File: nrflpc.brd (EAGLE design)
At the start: 67.9 x 42 mm, 74 parts, among them IC1 LPC1111/12/13/14-HVQFN33, IC2 LT1763CS8-3.3, IC3 LM3401, IC5 LM3401, IC6 LM3401, IC7 LM3401, Q1 20MHz, Q2 MOSFET-PCHANNEL, Q3 MOSFET-PCHANNEL, Q4 MOSFET-PCHANNEL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

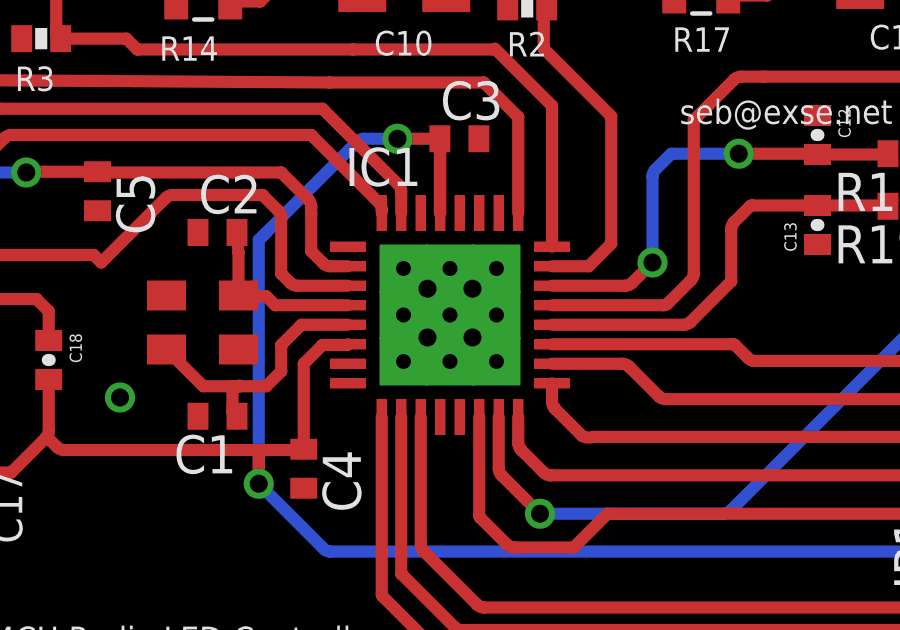
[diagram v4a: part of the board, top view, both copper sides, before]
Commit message: updated HVQFN33 package
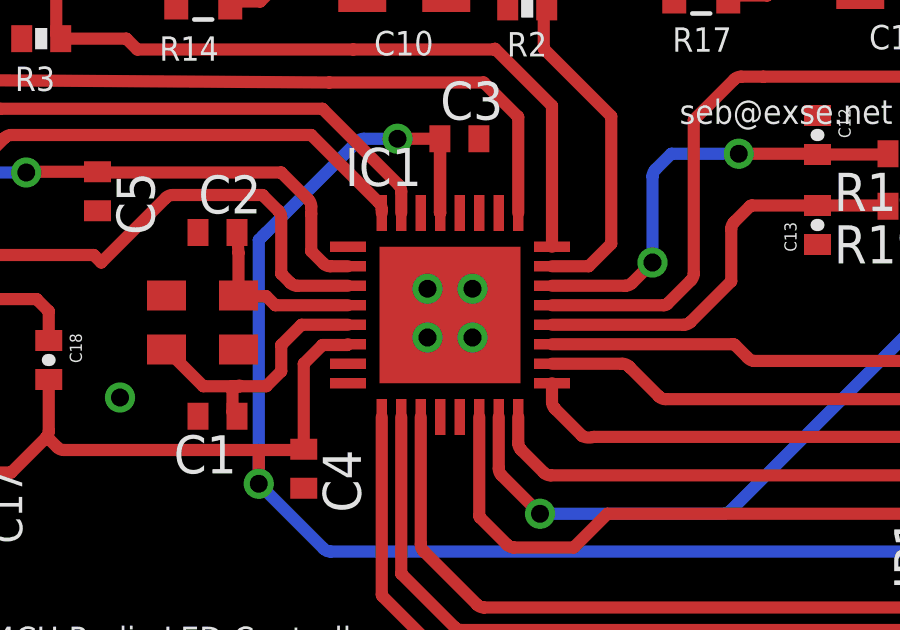
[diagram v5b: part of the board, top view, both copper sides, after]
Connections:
- net GND: now also IC1.GND; no longer IC1.33
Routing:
- net GND: track 17.8 -> 19.3 mm
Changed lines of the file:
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@@
 <contactref element="C2" pad="1"/>
 <contactref element="C1" pad="2"/>
-<contactref element="IC1" pad="33"/>
+<contactref element="IC1" pad="GND"/>
 <contactref element="C4" pad="2"/>
 <contactref element="C3" pad="2"/>
@@
 <contactref element="EXT" pad="7"/>
 <via x="21.625" y="6" extent="1-16" drill="0.6"/>
-<wire x1="32.625" y1="8.75" x2="33.375" y2="9.625" width="0" layer="19" extent="1-1"/>
-<wire x1="33.375" y1="8" x2="32.625" y2="8.75" width="0" layer="19" extent="1-1"/>
-<wire x1="31.875" y1="8" x2="32.625" y2="8.75" width="0" layer="19" extent="1-1"/>
-<wire x1="31.875" y1="9.625" x2="32.625" y2="8.75" width="0" layer="19" extent="1-1"/>
-<wire x1="33.5875" y1="14.625" x2="33.375" y2="9.625" width="0" layer="19" extent="1-1"/>
-<wire x1="34.549" y1="19.0205" x2="33.5875" y2="14.625" width="0" layer="19" extent="1-1"/>
 <wire x1="44.875" y1="11.1" x2="44.875" y2="15.4" width="0" layer="19" extent="1-1"/>
+<wire x1="33.5875" y1="14.625" x2="34.549" y2="19.0205" width="0" layer="19" extent="1-1"/>
+<wire x1="32.625" y1="8.75" x2="31.875" y2="8.75" width="0.4064" layer="1"/>
+<wire x1="31.875" y1="8.75" x2="31.875" y2="8" width="0.4064" layer="1"/>
 </signal>
 <signal name="N$1">

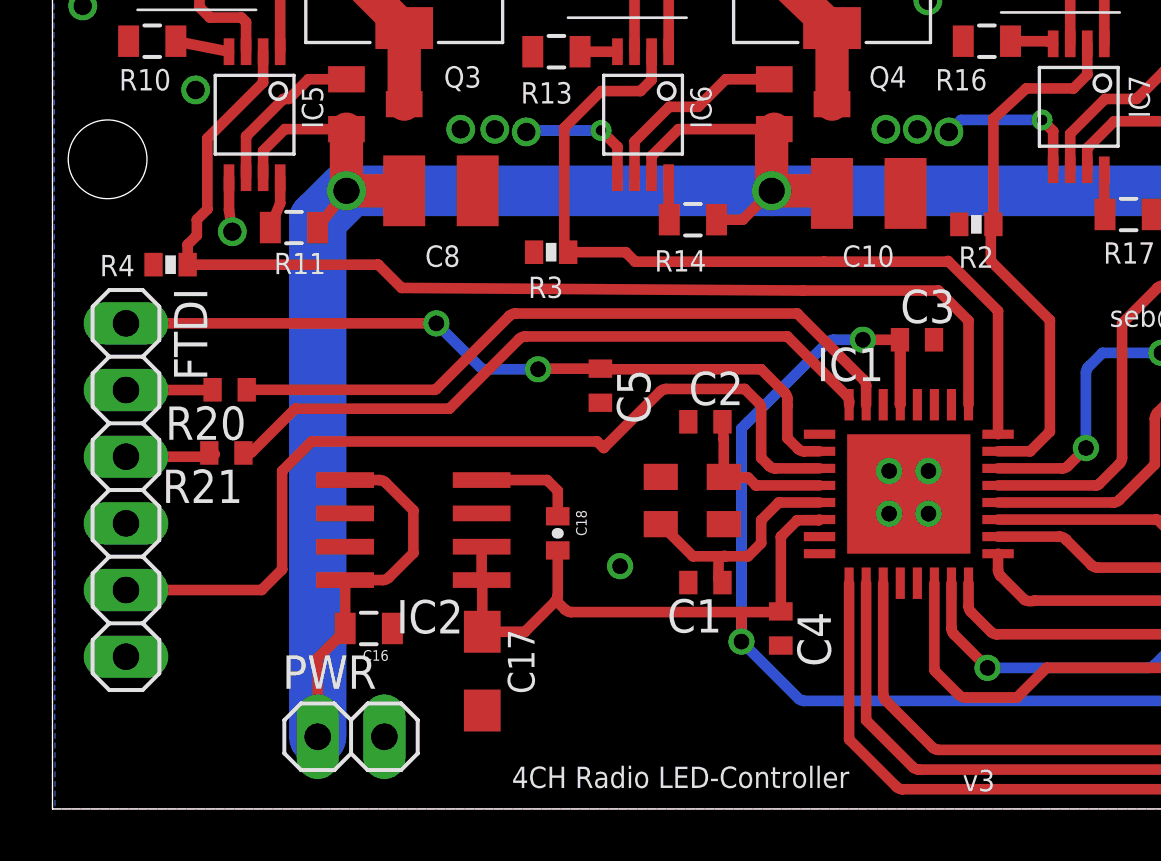
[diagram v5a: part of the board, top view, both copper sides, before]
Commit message: Compacting left side
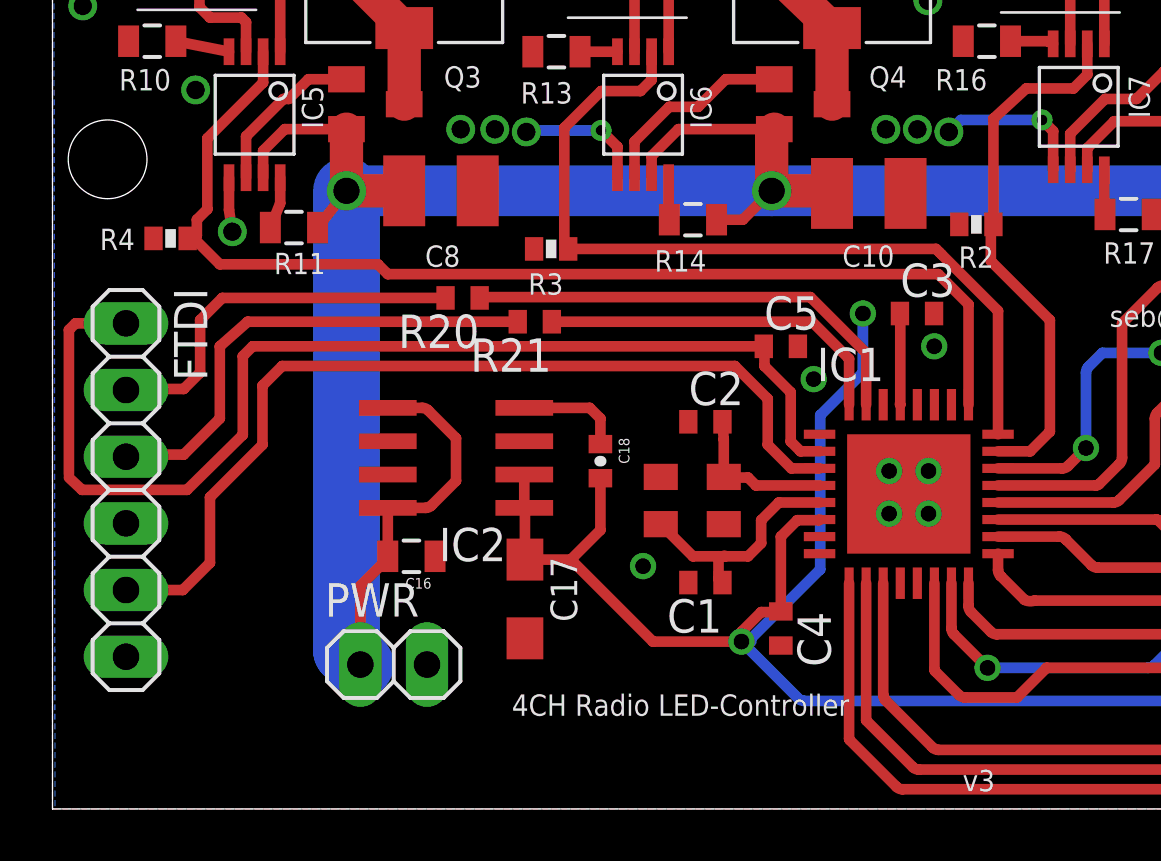
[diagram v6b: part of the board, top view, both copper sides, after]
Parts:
- moved R21 12.8 mm to (18.4, 15.3)
- moved R20 9.54 mm to (15.6, 16.2)
- moved C5 7.04 mm to (27.8, 14.4), turned to 0 degrees
- moved C16 3.19 mm to (13.7, 6.38)
- moved C17 3.19 mm to (18.0, 4.75)
- moved C18 3.19 mm to (20.9, 10.0)
- moved IC2 3.19 mm to (15.4, 10.1)
- moved PWR 3.19 mm to (13.0, 2.25)
- moved C3 1.00 mm to (32.9, 15.6)
- moved R4 1.00 mm to (4.50, 18.5)
- moved R3 0.12 mm to (19.0, 18.1)
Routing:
- net TXD: track 3.60 -> 18.6 mm
- net !RST: track 29.3 -> 43.8 mm, vias 2 -> 0
- net N$30: track 26.1 -> 13.7 mm
- net RXD: track 3.51 -> 14.8 mm
- net N$27: track 26.7 -> 17.6 mm
- net +12V: track 135.3 -> 132.3 mm
- net +3V3: track 98.4 -> 96.6 mm
- net BOOTL: track 34.4 -> 35.4 mm
- net GND: vias 46 -> 48

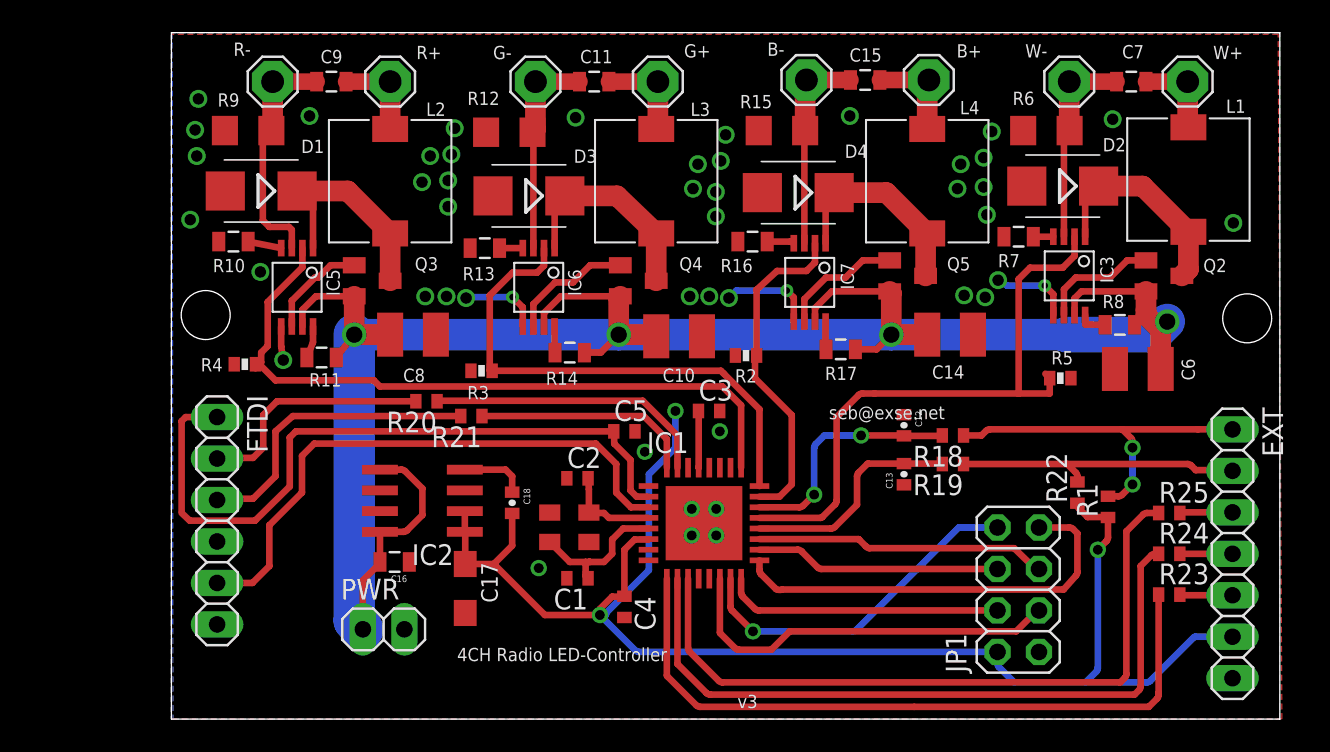
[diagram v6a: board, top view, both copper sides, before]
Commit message: Compacted right side, reset switch added
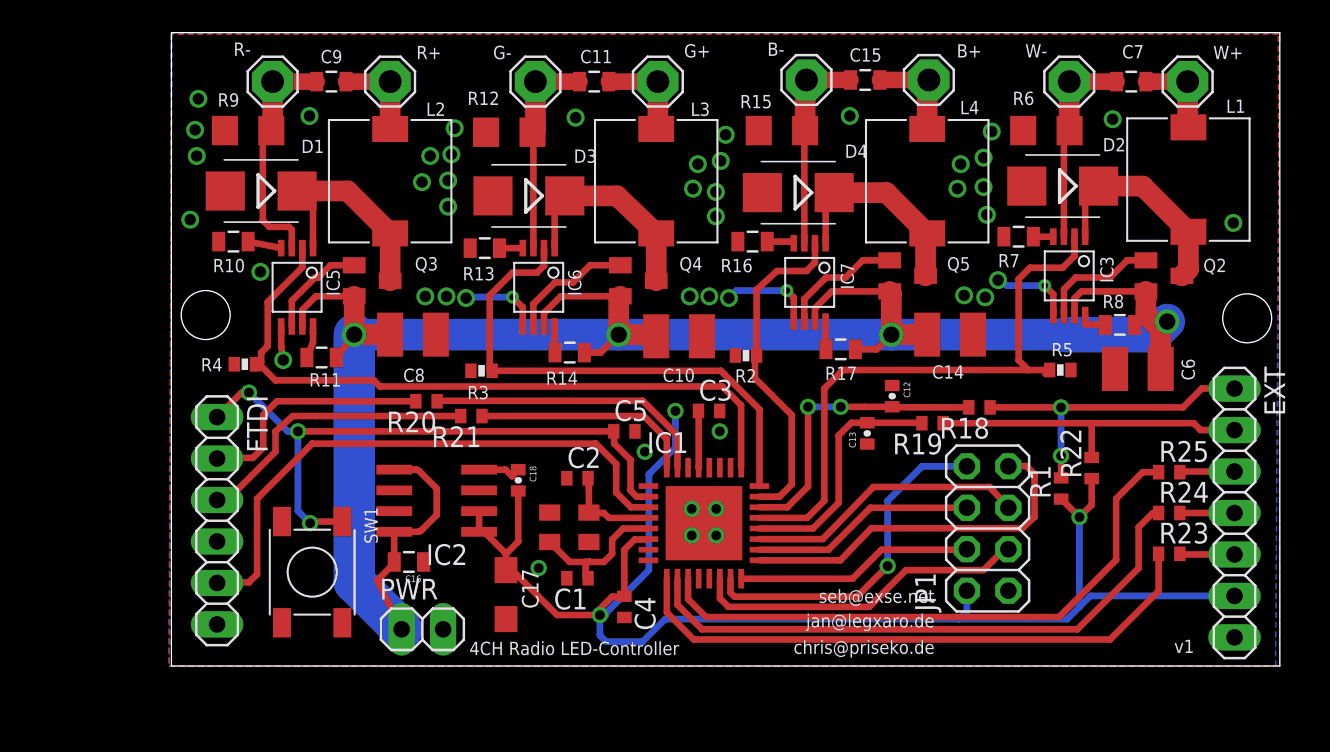
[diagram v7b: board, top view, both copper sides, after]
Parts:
- added SW1: SWITCH_SKQG, seb:SWITCH_SKQG
- moved JP1 4.19 mm to (50.0, 8.43)
- moved C13 3.36 mm to (42.6, 14.2)
- moved R1 3.09 mm to (54.5, 10.9)
- moved R19 2.80 mm to (46.6, 14.9)
- moved C17 2.53 mm to (20.5, 4.38)
- moved EXT 2.50 mm to (65.1, 9.38)
- moved R23 2.50 mm to (61.1, 6.88)
- moved R24 2.50 mm to (61.1, 9.38)
- moved R25 2.50 mm to (61.1, 11.9)
- moved PWR 2.38 mm to (15.4, 2.25)
- moved R18 2.37 mm to (49.5, 15.8)
- moved C12 1.92 mm to (44.2, 16.5)
- moved R22 1.74 mm to (56.4, 12.1)
- moved C18 1.43 mm to (21.2, 11.4)
- moved C16 0.88 mm to (14.6, 6.38)
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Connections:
- net !RST: now also SW1.1A
- net GND: now also SW1.2A
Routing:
- net N$35: track 43.4 -> 36.1 mm
- net N$36: track 43.4 -> 36.4 mm
- net N$34: track 43.3 -> 36.4 mm
- net !RST: track 43.8 -> 39.2 mm, vias 0 -> 3
- net CE: track 24.2 -> 20.5 mm
- net MISO: track 26.0 -> 22.4 mm
- net AD1: track 14.7 -> 18.2 mm
- net +3V3: track 96.6 -> 93.8 mm
- net CSN: track 17.1 -> 14.6 mm
- net AIN0: track 22.0 -> 19.8 mm
- net AIN1: track 18.0 -> 20.2 mm
- net +12V: track 132.3 -> 133.7 mm
- net N$18: track 4.04 -> 2.74 mm
- net MOSI: track 15.0 -> 13.8 mm
- net AD6: track 13.9 -> 15.1 mm
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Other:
- board size 67.9 x 42 mm -> 67.9 x 38.8 mm
- board text added: "chris@priseko.de"
- board text added: "jan@legxaro.de"
- board text added: "v1"
- board text removed: "v3"

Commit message: Labels and Makeup
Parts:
- renumbered JP1 to NRF, SW1 to RESET
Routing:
- net +12V: track 133.7 -> 133.1 mm
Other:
- board text added: "3V3"
- board text added: "AIN0"
- board text added: "AIN1"
- board text added: "GND"
- board text added: "IO0"
- board text added: "IO1"
- board text added: "IO2"
- board text removed: "IC2"
